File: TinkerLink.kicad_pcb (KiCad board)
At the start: 2 copper layers, 40 x 24 mm, 20 parts, among them J1 Conn_01x06_Pin, Q1 IRF4905S, Q2 MMBT2222A, SW1 TS-061D-250D4-P, U1 ESP-01F-2M, U2 ME6211C33M5

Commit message: new 3v3 in place(ish)
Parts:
- removed C1, C2: 10uf, Capacitor_SMD:C_0603_1608Metric
- removed Rshunt: 0R1 1%, Resistor_SMD:R_2512_6332Metric
- removed U2: ME6211C33M5, Package_TO_SOT_SMD:SOT-23-5
- added C5: 10uf, Capacitor_SMD:C_0603_1608Metric, F.Cu at (99.5, 110.8)
- added C6: 100nf, Capacitor_SMD:C_0603_1608Metric, F.Cu at (105.9, 110.0)
- added C7: 22uF, Capacitor_SMD:C_0603_1608Metric, F.Cu at (108.8, 110.0)
- added C8: 22uF, Capacitor_SMD:C_0603_1608Metric, F.Cu at (99.6, 109.3)
- added L2: 3.9uH, Inductor_SMD:L_0603_1608Metric, F.Cu at (107.4, 110.0)
- added Rsh1: 0R1 1%, Resistor_SMD:R_2512_6332Metric, F.Cu at (86.4, 109.7)
- added U3: AP63203WU, Package_TO_SOT_SMD:TSOT-23-6, F.Cu at (103.1, 110.0)
- moved R6 3.26 mm to (113.5, 107.7), turned to 0 degrees
- moved J1 2.06 mm to (91.0, 106.0)
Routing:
- net Vdd: track 45.2 -> 50.2 mm
- net Net-(U3-SW): track 0.00 -> 3.47 mm
- net /Vbus: track 39.2 -> 42.6 mm, vias 7 -> 5
- net /RST: track 5.19 -> 2.98 mm
- net /io0: track 8.49 -> 6.40 mm
- net /Rx: track 5.33 -> 3.51 mm
- net /Tx: track 4.90 -> 3.10 mm
- net Net-(U3-BST): track 0.00 -> 1.72 mm
- net io4: vias 3 -> 2

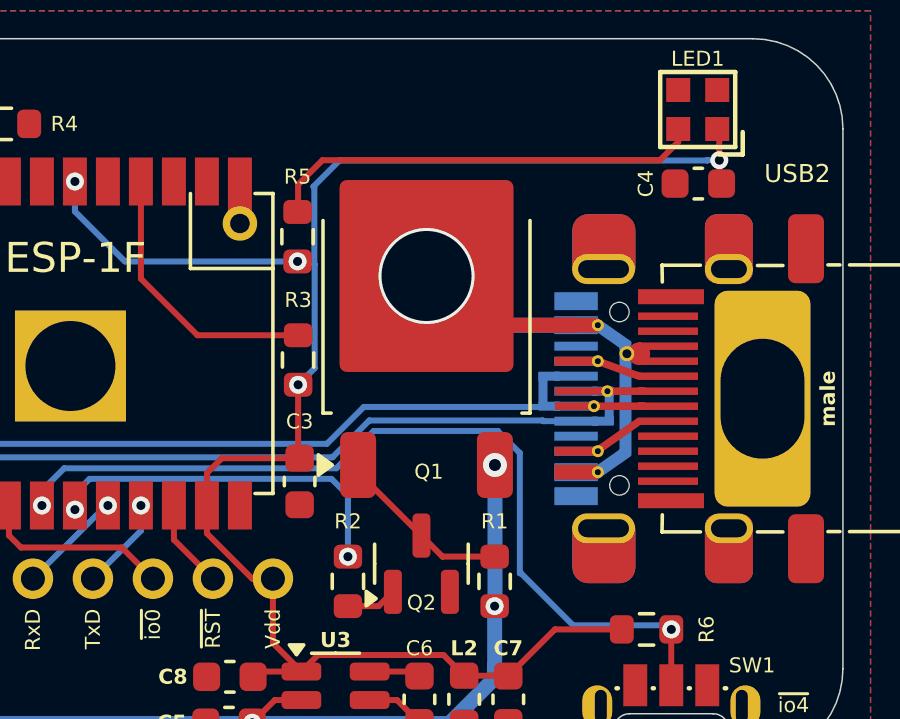
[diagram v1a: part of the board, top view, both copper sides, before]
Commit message: Austin instigated FET change
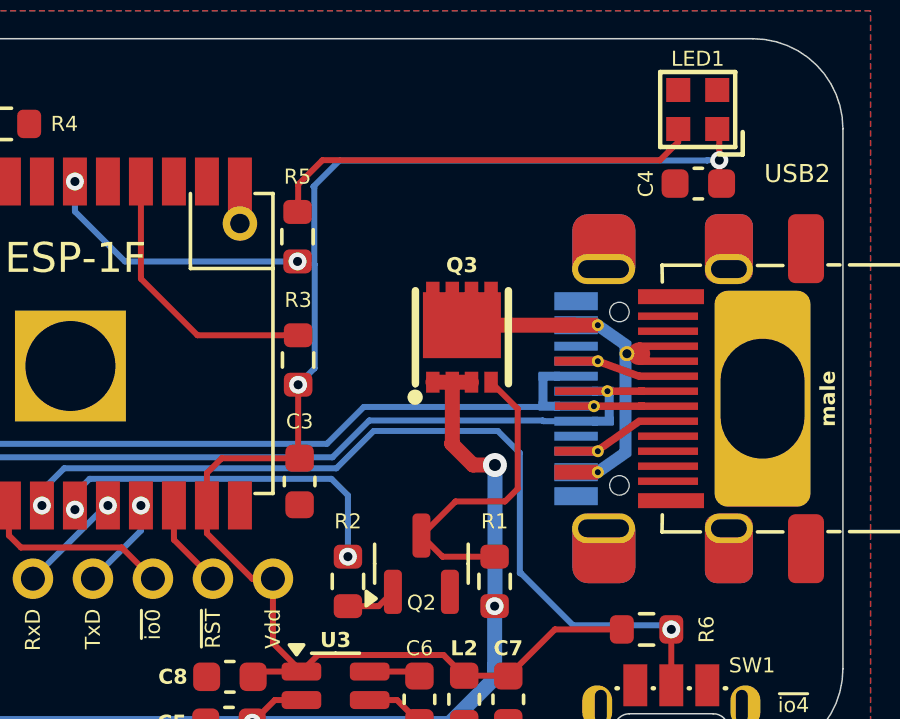
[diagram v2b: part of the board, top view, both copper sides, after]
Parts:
- removed Q1: IRF4905S, Package_TO_SOT_SMD:TO-252-2
- added Q3: SQS411ENW-T1_GE3, LCSCfootprints:POWERPAK-1212-8_L3.1-W3.1-P0.65-LS3.3-BL, F.Cu at (107.3, 98.0)
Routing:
- net /VbusS: track 12.2 -> 3.81 mm, vias 1 -> 0
- net /Vbus: track 42.6 -> 47.7 mm
- net Net-(Q2-C): track 5.96 -> 10.5 mm

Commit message: squish...
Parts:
- moved R1 5.22 mm to (108.1, 100.9), turned to 0 degrees
- moved Rsh1 3.85 mm to (90.2, 109.8)
- moved R2 3.78 mm to (107.2, 106.9), turned to 180 degrees
- moved R6 3.14 mm to (110.4, 108.4), turned to 90 degrees
- moved R3 3.06 mm to (104.7, 97.7)
- moved R5 2.98 mm to (104.7, 94.0)
- moved J1 2.92 mm to (93.9, 106.0)
- moved U1 2.92 mm to (98.4, 98.2)
- moved C3 2.84 mm to (104.7, 102.7)
- moved R4 2.78 mm to (94.8, 90.8)
- moved Q2 2.44 mm to (108.0, 104.2)
- moved C4 1.45 mm to (116.5, 92.2)
- moved LED1 1.39 mm to (116.5, 90.0)
- moved Q3 0.74 mm to (108.0, 98.2)
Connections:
- J1 pad 2: /Rx -> /io0
- J1 pad 3: /Tx -> /Rx
- J1 pad 4: /io0 -> /Tx
- USB1 pad A5: unconnected-(USB1-PadA5) -> Vconn
- USB1 pad B5: unconnected-(USB1-PadB5) -> CC
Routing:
- net CC: track 0.00 -> 25.8 mm
- net Vconn: track 0.00 -> 25.3 mm
- net Vdd: track 50.2 -> 43.1 mm
- net io4: track 29.3 -> 22.4 mm
- net Net-(Q2-C): track 10.5 -> 3.95 mm
- net /io0: track 6.40 -> 2.77 mm
- net /Vbus: track 47.7 -> 44.7 mm, vias 5 -> 4
- net /VbusS: track 3.81 -> 6.41 mm, vias 0 -> 1
- net i05: track 12.1 -> 11.2 mm
- net /Rx: track 3.51 -> 2.65 mm, vias 1 -> 0
- net /EN: track 9.26 -> 8.48 mm
- net io14: track 9.11 -> 9.66 mm
- net Net-(Q2-B): track 1.70 -> 2.20 mm
- net /Tx: track 3.10 -> 2.61 mm, vias 1 -> 0

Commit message: Dual FETs
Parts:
- added Q4: SQS411ENW-T1_GE3, LCSCfootprints:POWERPAK-1212-8_L3.1-W3.1-P0.65-LS3.3-BL, F.Cu at (108.0, 95.6)
- moved C8 4.84 mm to (94.7, 109.0)
- moved C5 4.81 mm to (94.7, 110.6)
- moved U3 4.69 mm to (98.4, 109.8)
- moved L2 4.56 mm to (102.8, 109.8)
- moved C6 4.55 mm to (101.3, 109.8)
- moved C7 4.54 mm to (104.3, 109.8)
- moved Rsh1 2.43 mm to (87.8, 109.7)
- moved R1 1.81 mm to (108.0, 102.7)
- moved Q3 1.70 mm to (108.0, 99.9)
- moved R6 1.44 mm to (110.1, 109.8)
- moved Q2 1.24 mm to (108.0, 105.4)
- moved R2 1.18 mm to (107.1, 108.1)
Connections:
- Q3 pad 5: /VbusS -> Net-(Q3-D-Pad5)
- Q3 pad 6: /VbusS -> Net-(Q3-D-Pad5)
- Q3 pad 7: /VbusS -> Net-(Q3-D-Pad5)
- Q3 pad 8: /VbusS -> Net-(Q3-D-Pad5)
- Q3 pad 9: /VbusS -> Net-(Q3-D-Pad5)
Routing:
- net Net-(Q2-C): track 3.95 -> 15.0 mm
- net Vdd: track 43.1 -> 50.3 mm, vias 2 -> 4
- net Net-(Q3-D-Pad5): track 0.00 -> 5.00 mm
- net /VbusS: track 6.41 -> 11.3 mm
- net /Vbus: track 44.7 -> 41.9 mm
- net io4: track 22.4 -> 23.7 mm
- net i05: track 11.2 -> 12.4 mm

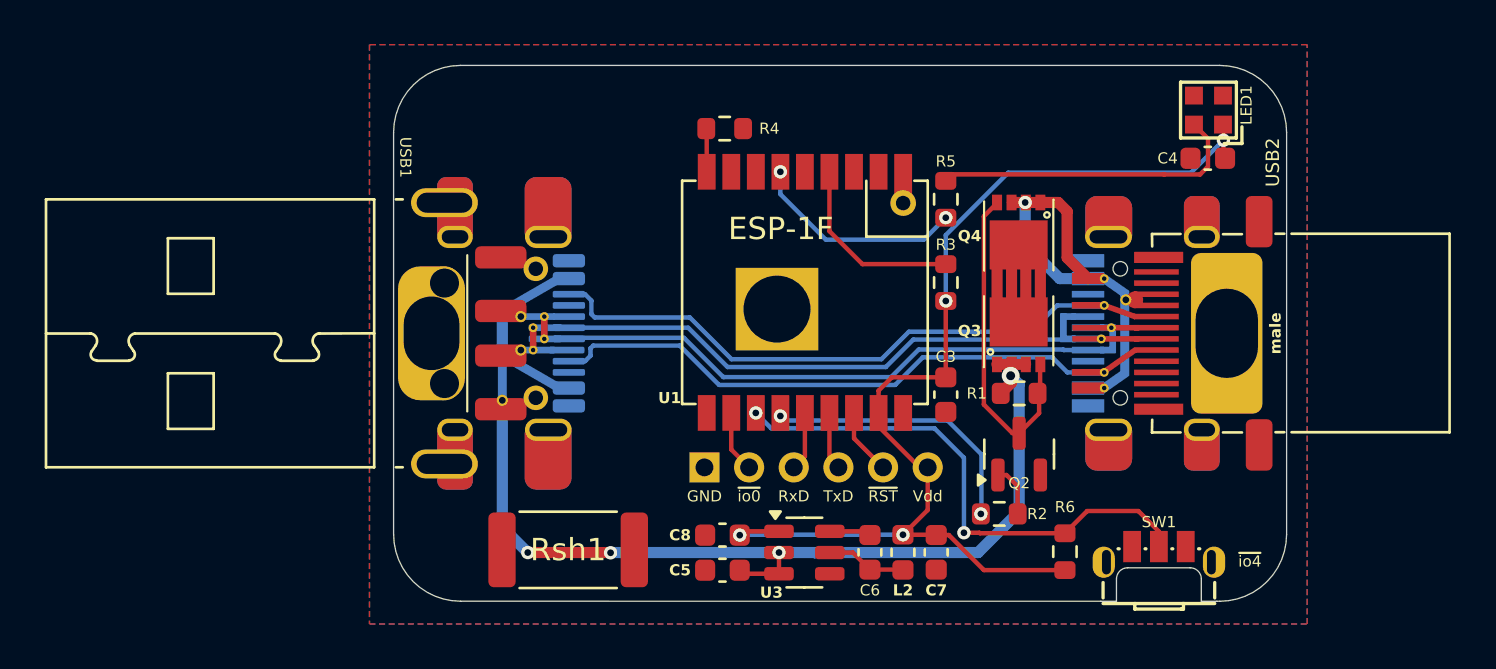
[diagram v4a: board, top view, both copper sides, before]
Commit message: upgrades
adds ina228 and 3535 rgbw sk6812 LED
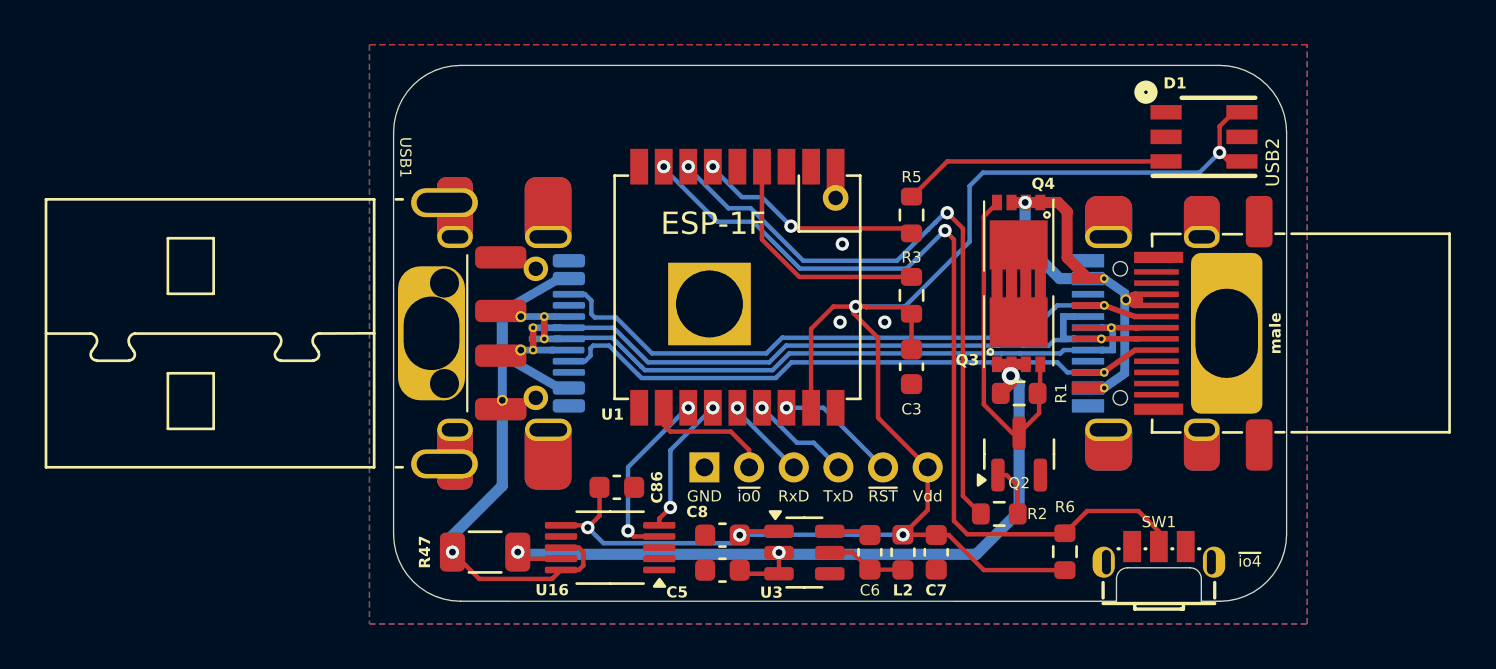
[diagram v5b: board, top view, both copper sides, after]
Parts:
- removed C4: 10uf, Capacitor_SMD:C_0603_1608Metric
- removed LED1: SK6812-EC20, LCSCfootprints:LED-SMD_4P-L2.0-W2.0-BR
- removed R4: 10K, Resistor_SMD:R_0603_1608Metric
- removed Rsh1: 0R1 1%, Resistor_SMD:R_2512_6332Metric
- added C86: 100nf, Capacitor_SMD:C_0603_1608Metric, F.Cu at (90.0, 106.9)
- added D1: ~, AC_LED:SK6812MINIRGBWNWP6, F.Cu at (116.3, 91.2)
- added R47: 2mR 1w, Resistor_SMD:R_1206_3216Metric, F.Cu at (84.1, 109.8)
- added U16: INA228, Package_SO:VSSOP-10_3x3mm_P0.5mm, F.Cu at (89.7, 109.6)
- moved U1 3.03 mm to (95.4, 97.9)
- moved C3 1.98 mm to (103.2, 101.5)
- moved R5 1.69 mm to (103.2, 94.7)
- moved R3 1.64 mm to (103.2, 98.3)
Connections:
- C5 pad 1: /Vbus -> /VbusX
- Q3 pad 1: /Vbus -> /VbusX
- Q3 pad 2: /Vbus -> /VbusX
- Q3 pad 3: /Vbus -> /VbusX
- R1 pad 1: /Vbus -> /VbusX
- R2 pad 2: i05 -> io12
- R6 pad 2: io4 -> io13
- SW1 pad 2: io4 -> io13
- U1 pad 9: /io15 -> io15
- U3 pad 2: /Vbus -> /VbusX
- U3 pad 3: /Vbus -> /VbusX
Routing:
- net io13: track 0.00 -> 39.3 mm, vias 0 -> 2
- net /VbusX: track 0.00 -> 37.2 mm, vias 0 -> 3
- net io12: track 0.00 -> 28.4 mm, vias 0 -> 2
- net /Vbus: track 41.9 -> 16.0 mm, vias 4 -> 1
- net Vdd: track 50.3 -> 73.9 mm, vias 4 -> 5
- net io4: track 23.7 -> 8.21 mm
- net i05: track 12.4 -> 6.26 mm
- net /io0: track 2.77 -> 5.84 mm
- net Net-(D1-DIN): track 14.6 -> 12.1 mm
- net /RST: track 2.98 -> 5.43 mm, vias 0 -> 1
- net /EN: track 8.48 -> 10.7 mm
- net /Tx: track 2.61 -> 4.53 mm, vias 0 -> 1
- net /io15: track 1.80 -> 0.00 mm
- net /Rx: track 2.65 -> 3.72 mm, vias 0 -> 1
- net io14: track 9.66 -> 10.2 mm
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
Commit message: add AC logo
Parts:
- added LOGO1: Creations_logo_med, AC_logos:Creations logo med, B.Cu at (104.3, 95.6)

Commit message: first tweaks post Austin...
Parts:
- added REF**: DagNabbit, tinker:DagNabbit, B.Cu at (108.4, 106.2)
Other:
- board text added: "${COMPANY} ${COMMENT1}"

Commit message: ...
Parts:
- removed D1: ~, AC_LED:SK6812MINIRGBWNWP6
- added LED1: SK6812MINIRGBW-WS-P6-A, LCSCfootprints:LED-SMD_6P-L3.5-W3.5_SK6812MINIRGBW-WS-P6-A, F.Cu at (116.3, 91.2)
- LOGO1: footprint AC_logos:Creations logo med -> LCSCfootprints:Creations logo med
